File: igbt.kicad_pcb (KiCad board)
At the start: 2 copper layers, 31 parts, among them J1 PWM, J3 Sense_AC, Q1 IRG4PF50W, Q2 IRG4PF50W, Q3 IRG4PF50W, Q4 IRG4PF50W, Q5 IRG4PF50W, Q6 IRG4PF50W, U1 ACS758xCB-050B-PFF, U2 ACS758xCB-050B-PFF

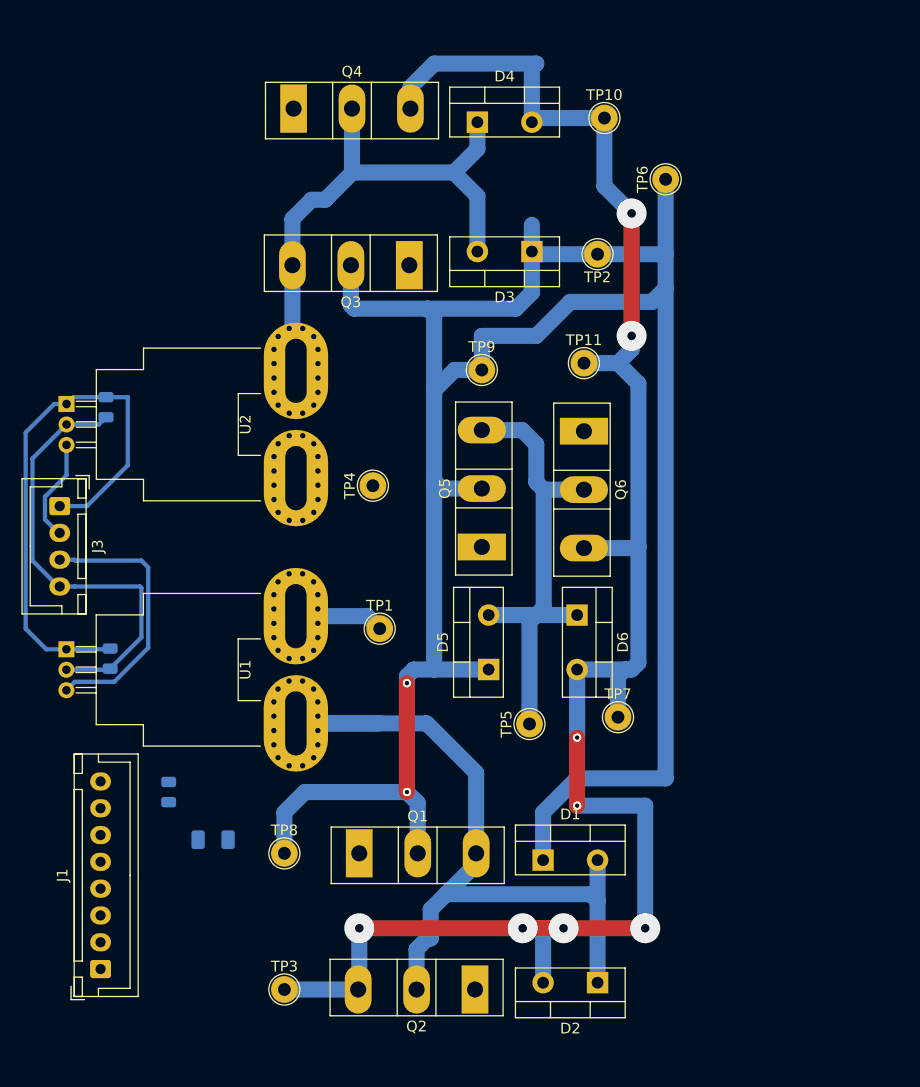
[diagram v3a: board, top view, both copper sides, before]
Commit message: Schematic for sandwitch board with drivers
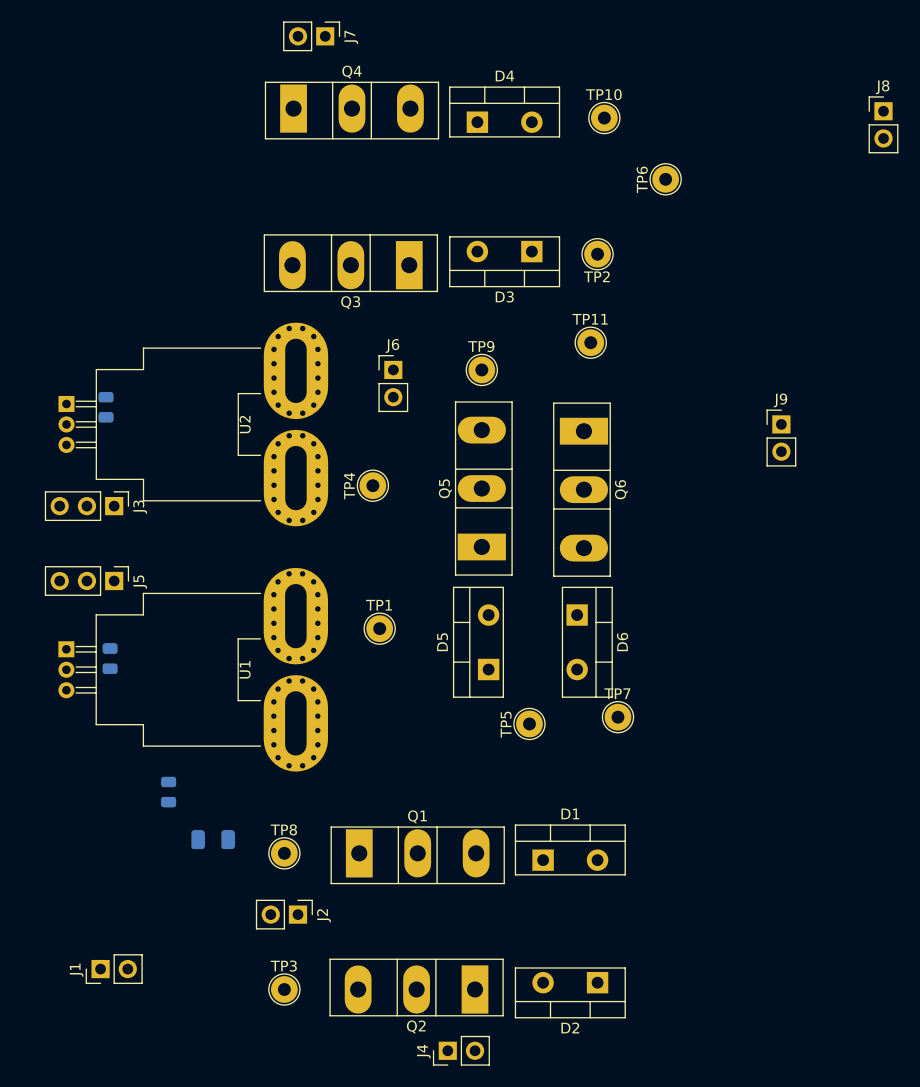
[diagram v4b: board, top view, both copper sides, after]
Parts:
- added J2: A_Top, Connector_PinHeader_2.54mm:PinHeader_1x02_P2.54mm_Vertical, F.Cu at (61.6, 159.4)
- added J4: A_Bottom, Connector_PinHeader_2.54mm:PinHeader_1x02_P2.54mm_Vertical, F.Cu at (75.6, 172.1)
- added J5: Sense_AC_A, Connector_PinHeader_2.54mm:PinHeader_1x03_P2.54mm_Vertical, F.Cu at (44.5, 128.3)
- added J6: B_Top, Connector_PinHeader_2.54mm:PinHeader_1x02_P2.54mm_Vertical, F.Cu at (70.5, 108.6)
- added J7: B_Bottom, Connector_PinHeader_2.54mm:PinHeader_1x02_P2.54mm_Vertical, F.Cu at (64.1, 77.5)
- added J8: C_Top, Connector_PinHeader_2.54mm:PinHeader_1x02_P2.54mm_Vertical, F.Cu at (116.2, 84.5)
- added J9: C_Bottom, Connector_PinHeader_2.54mm:PinHeader_1x02_P2.54mm_Vertical, F.Cu at (106.7, 113.7)
- J1: value PWM -> DC_Sense; footprint Connector_JST:JST_XH_B08B-XH-A_1x08_P2.50mm_Vertical -> Connector_PinHeader_2.54mm:PinHeader_1x02_P2.54mm_Vertical
- J3: value Sense_AC -> Sense_AC_B; footprint Connector_JST:JST_XH_B04B-XH-A_1x04_P2.50mm_Vertical -> Connector_PinHeader_2.54mm:PinHeader_1x03_P2.54mm_Vertical
- moved J3 5.08 mm to (44.5, 121.3)
- moved TP11 2.01 mm to (88.9, 106.0)
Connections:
- C5 pad 2: Net-(C4-Pad1) -> Net-(C5-Pad2)
- J1 pad 1: Net-(J1-Pad1) -> Net-(D2-Pad2)
- J1 pad 2: Net-(J1-Pad2) -> /bus_sense
- J3 pad 1: Net-(C4-Pad1) -> GND
- J3 pad 3: Net-(J3-Pad3) -> Net-(C5-Pad2)
- Q1 pad 1: Net-(J1-Pad1) -> Net-(J2-Pad2)
- Q2 pad 1: Net-(J1-Pad2) -> Net-(J4-Pad2)
- Q3 pad 1: Net-(J1-Pad3) -> Net-(J6-Pad2)
- Q4 pad 1: Net-(J1-Pad4) -> Net-(J7-Pad2)
- Q5 pad 1: Net-(J1-Pad5) -> Net-(J8-Pad2)
- Q6 pad 1: Net-(J1-Pad6) -> Net-(J9-Pad2)
- R7 pad 1: Net-(J1-Pad7) -> /bus_sense
- R8 pad 2: Net-(J1-Pad7) -> /bus_sense
- U1 pad 3: Net-(J3-Pad3) -> Net-(J5-Pad2)
- U2 pad 1: Net-(C4-Pad1) -> Net-(C5-Pad2)
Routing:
- net Net-(D1-Pad1): track 220.2 -> 0.00 mm, vias 2 -> 0
- net Net-(D2-Pad2): track 178.0 -> 0.00 mm, vias 8 -> 0
- net Net-(D1-Pad2): track 75.0 -> 0.00 mm
- net Net-(C4-Pad1): track 52.2 -> 0.00 mm
- net Net-(D3-Pad2): track 51.0 -> 0.00 mm
- net Net-(D5-Pad2): track 44.6 -> 0.00 mm
- net GND: track 42.1 -> 0.00 mm
- net Net-(J3-Pad3): track 25.3 -> 0.00 mm
- net Net-(J3-Pad2): track 9.68 -> 0.00 mm
- net Net-(TP1-Pad1): track 8.30 -> 0.00 mm

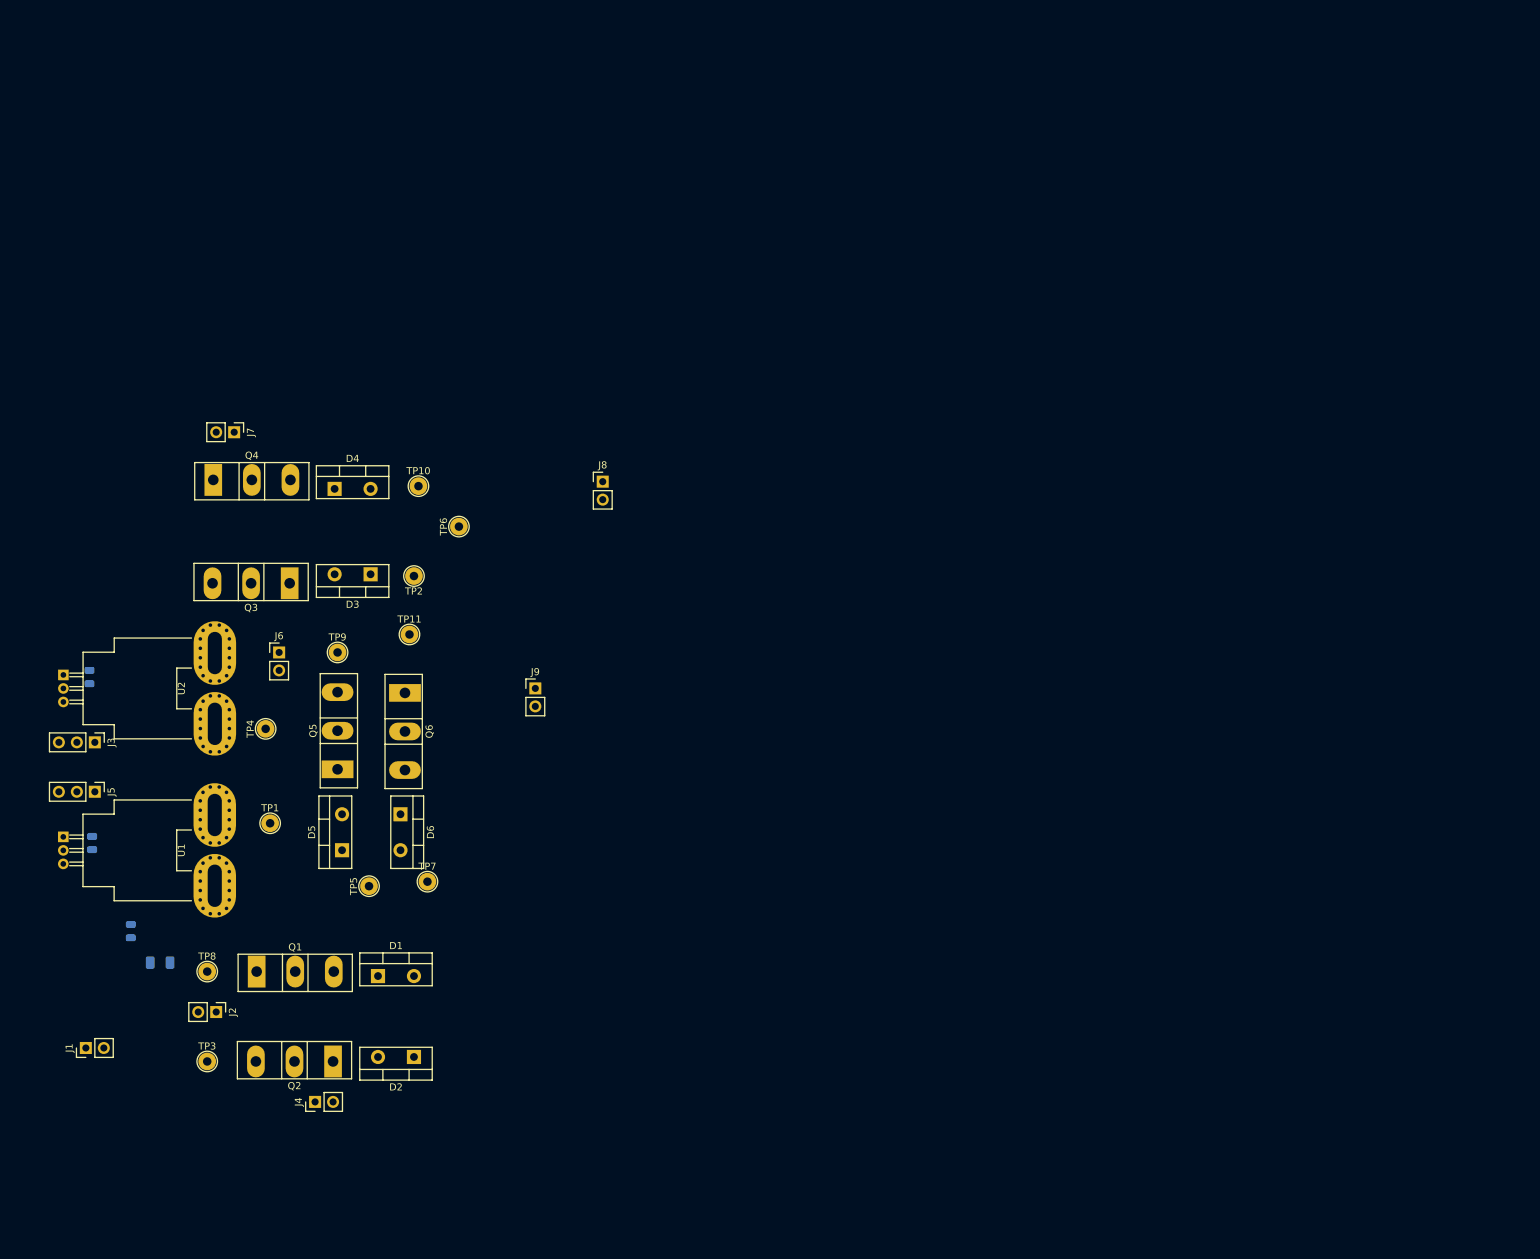
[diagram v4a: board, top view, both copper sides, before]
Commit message: Tabs on top, I sensor swapped for wasy routing
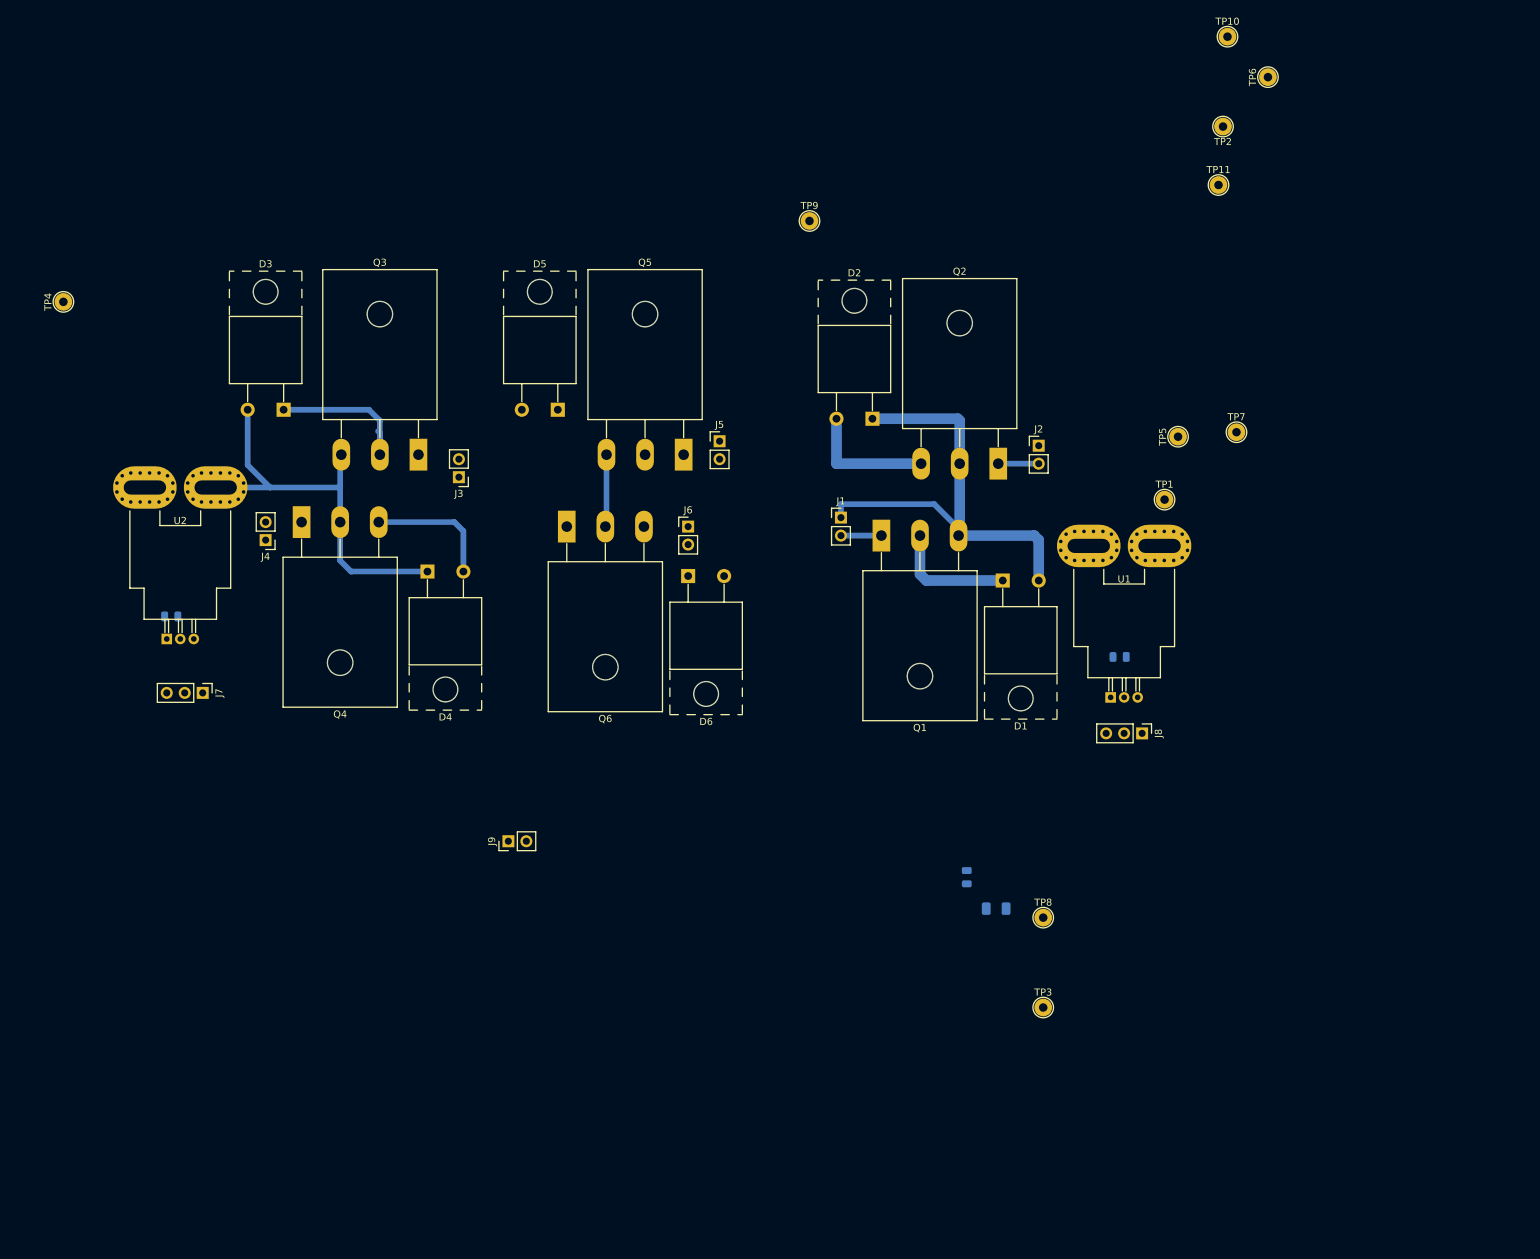
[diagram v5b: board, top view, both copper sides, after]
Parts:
- removed the J5 at (44.5, 128.3)
- removed the J9 at (106.7, 113.7)
- added J6: C_Bottom, Connector_PinHeader_2.54mm:PinHeader_1x02_P2.54mm_Vertical, F.Cu at (128.3, 90.8)
- added J8: Sense_AC_A, Connector_PinHeader_2.54mm:PinHeader_1x03_P2.54mm_Vertical, F.Cu at (192.4, 120.0)
- D1, D2, D3, D4, D5, D6: footprint Package_TO_SOT_THT:TO-220-2_Vertical -> Package_TO_SOT_THT:TO-220-2_Horizontal_TabUp
- Q1, Q2, Q3, Q4, Q5, Q6: footprint Package_TO_SOT_THT:TO-247-3_Vertical -> Package_TO_SOT_THT:TO-247-3_Horizontal_TabUp
- moved U1 149.3 mm to (188.0, 114.9), turned to 0 degrees
- moved C4 147.5 mm to (189.2, 109.2), turned to 0 degrees
- moved J2 138.0 mm to (177.8, 79.4), turned to 0 degrees
- moved TP1 134.4 mm to (195.6, 87.0)
- moved TP2 130.8 mm to (203.8, 34.3)
- moved TP7 130.8 mm to (205.7, 77.5)
- moved TP10 130.8 mm to (204.5, 21.6)
- moved TP11 130.8 mm to (203.2, 42.5)
- moved TP5 130.8 mm to (197.5, 78.1)
- moved TP6 130.8 mm to (210.2, 27.3)
- moved Q2 126.4 mm to (172.1, 81.9)
- moved R7 118.4 mm to (171.8, 144.8)
- moved TP3 118.4 mm to (178.4, 158.8)
- moved TP8 118.4 mm to (178.4, 146.1)
- moved R8 118.4 mm to (167.6, 140.3)
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- renumbered J2 to J1, J4 to J2, J6 to J3, J7 to J4, J8 to J5, J3 to J7, J1 to J9
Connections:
- C4 pad 2: GND -> Net-(C4-Pad2)
- C5 pad 1: GND -> Net-(C5-Pad1)
- J7 pad 1: GND -> Net-(C5-Pad1)
- U1 pad 2: GND -> Net-(C4-Pad2)
- U1 pad 4: Net-(D1-Pad2) -> Net-(TP1-Pad1)
- U1 pad 5: Net-(TP1-Pad1) -> Net-(D1-Pad2)
- U2 pad 2: GND -> Net-(C5-Pad1)
- U2 pad 4: Net-(TP4-Pad1) -> Net-(D3-Pad2)
- U2 pad 5: Net-(D3-Pad2) -> Net-(TP4-Pad1)
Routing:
- net Net-(D1-Pad2): track 0.00 -> 67.0 mm
- net Net-(D3-Pad2): track 0.00 -> 58.0 mm
- net Net-(D1-Pad1): track 0.00 -> 40.0 mm
- net Net-(D2-Pad2): track 0.00 -> 36.5 mm
- net Net-(D5-Pad2): track 0.00 -> 10.2 mm
- net Net-(J2-Pad2): track 0.00 -> 5.72 mm
- net Net-(J1-Pad2): track 0.00 -> 5.71 mm

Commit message: placement
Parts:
- moved TP10 177.2 mm to (54.6, 116.2)
- moved TP2 160.0 mm to (45.1, 54.6)
- moved TP11 129.1 mm to (94.6, 112.4)
- moved TP8 101.7 mm to (130.2, 56.5)
- moved TP5 100.7 mm to (97.2, 86.4), turned to 0 degrees
- moved R7 90.2 mm to (175.3, 54.6), turned to 180 degrees
- moved J9 83.1 mm to (182.2, 110.5)
- moved TP3 62.4 mm to (134.6, 114.3)
- moved J8 60.0 mm to (175.2, 62.5), turned to 90 degrees
- moved TP9 56.4 mm to (89.5, 55.2)
- moved TP6 49.5 mm to (168.9, 54.6)
- moved U1 48.1 mm to (179.7, 67.6), turned to 180 degrees
- moved TP7 47.1 mm to (172.7, 111.1), turned to 180 degrees
- moved J2 43.0 mm to (137.2, 93.3), turned to 180 degrees
- moved D1 38.9 mm to (142.2, 74.3), turned to 180 degrees
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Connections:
- U1 pad 4: Net-(TP1-Pad1) -> Net-(D1-Pad2)
- U1 pad 5: Net-(D1-Pad2) -> Net-(TP1-Pad1)
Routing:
- net Net-(D1-Pad2): track 67.0 -> 0.00 mm
- net Net-(D3-Pad2): track 58.0 -> 0.00 mm
- net Net-(D1-Pad1): track 40.0 -> 0.00 mm
- net Net-(D2-Pad2): track 36.5 -> 0.00 mm
- net Net-(D5-Pad2): track 10.2 -> 0.00 mm
- net Net-(J2-Pad2): track 5.72 -> 0.00 mm
- net Net-(J1-Pad2): track 5.71 -> 0.00 mm

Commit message: Gate drive
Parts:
- moved TP6 45.8 mm to (214.6, 57.8)
- moved J6 23.6 mm to (96.5, 94.0), turned to 180 degrees
- moved TP7 20.1 mm to (191.8, 104.8)
- moved J1 6.38 mm to (165.7, 76.8)
- moved TP5 5.12 mm to (96.5, 81.3)
- moved J5 4.44 mm to (124.5, 83.8), turned to 180 degrees
- moved D2 3.81 mm to (160.7, 101.0)
- moved D4 3.17 mm to (79.4, 100.3)
- moved U1 2.62 mm to (179.1, 65.0)
- moved D6 2.62 mm to (119.4, 101.0)
- moved J8 2.62 mm to (174.6, 60.0)
- moved R7 2.62 mm to (174.6, 52.1)
- moved C4 2.62 mm to (177.8, 70.8)
- moved J2 1.42 mm to (135.9, 92.7)
- moved J3 1.42 mm to (85.1, 83.2)
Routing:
- net Net-(D1-Pad1): track 0.00 -> 239.7 mm
- net Net-(D2-Pad2): track 0.00 -> 175.0 mm
- net Net-(D1-Pad2): track 0.00 -> 90.5 mm
- net Net-(D3-Pad2): track 0.00 -> 79.3 mm
- net Net-(D5-Pad2): track 0.00 -> 42.0 mm
- net Net-(J1-Pad2): track 0.00 -> 17.0 mm
- net Net-(J2-Pad2): track 0.00 -> 7.25 mm
- net Net-(TP4-Pad1): track 0.00 -> 7.21 mm
- net Net-(J3-Pad2): track 0.00 -> 6.98 mm
- net Net-(J6-Pad2): track 0.00 -> 6.35 mm
- net Net-(J5-Pad2): track 0.00 -> 5.08 mm
- net Net-(J4-Pad2): track 0.00 -> 5.08 mm
